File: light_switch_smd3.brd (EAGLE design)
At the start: 37.1 x 45.2 mm, 17 parts, among them J2 SW1, T1 BT136, U1 LM1117

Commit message: light switch version 6 minor adjustments
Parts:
- removed AC, LAMP: DG306-5.0, myblog_library:DG306-PCKG
- added AC+LAMP: DG350-3.5-03P, myblog_library:DG350-3.5-03P
- moved R1 1.40 mm to (3.11, 10.9)
- moved R2 1.10 mm to (5.33, 10.9)
- moved U$2 0.94 mm to (10.8, 4.59)
- moved R5 0.80 mm to (7.49, 10.9)
- moved R6 0.61 mm to (9.81, 11.0)
- moved R4 0.60 mm to (12.3, 10.9)
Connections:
- net N$11: now also AC+LAMP.P$2; no longer AC.P$1, LAMP.P$2
- net N$12: now also AC+LAMP.P$3; no longer AC.P$2
- net N$8: now also AC+LAMP.P$1; no longer LAMP.P$1
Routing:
- net N$32: track 164.1 -> 151.4 mm
- net N$31: track 164.1 -> 151.6 mm
- net N$2: track 13.5 -> 7.16 mm
- net N$3: track 72.6 -> 67.1 mm
- net N$11: track 23.5 -> 19.0 mm
- net GND: track 7.86 -> 12.1 mm
- net N$12: track 24.8 -> 21.2 mm
- net N$4: track 17.9 -> 14.4 mm
- net N$8: track 18.8 -> 17.7 mm
- net N$1: track 16.8 -> 15.8 mm
- net N$5: track 12.0 -> 11.0 mm
- net N$9: track 6.99 -> 6.39 mm
- net N$14: track 4.20 -> 3.70 mm
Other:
- board size 37.1 x 45.2 mm -> 36.5 x 40.3 mm
- board text added: "Hristo Borisov Light Switch Prototype Rev. 0.6"
- board text removed: "Hristo Borisov Light Switch Prototype Rev. 0.5"

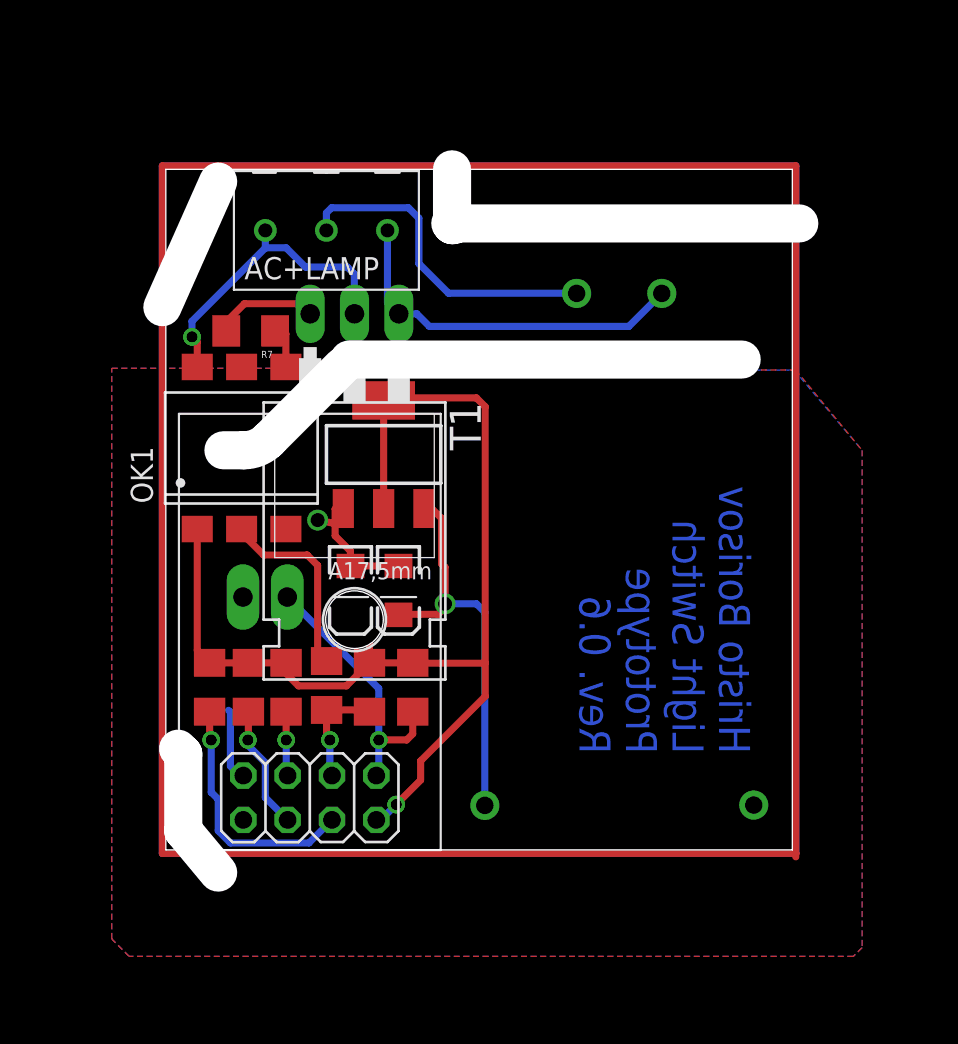
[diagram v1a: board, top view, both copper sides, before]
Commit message: Changing the BT136 device
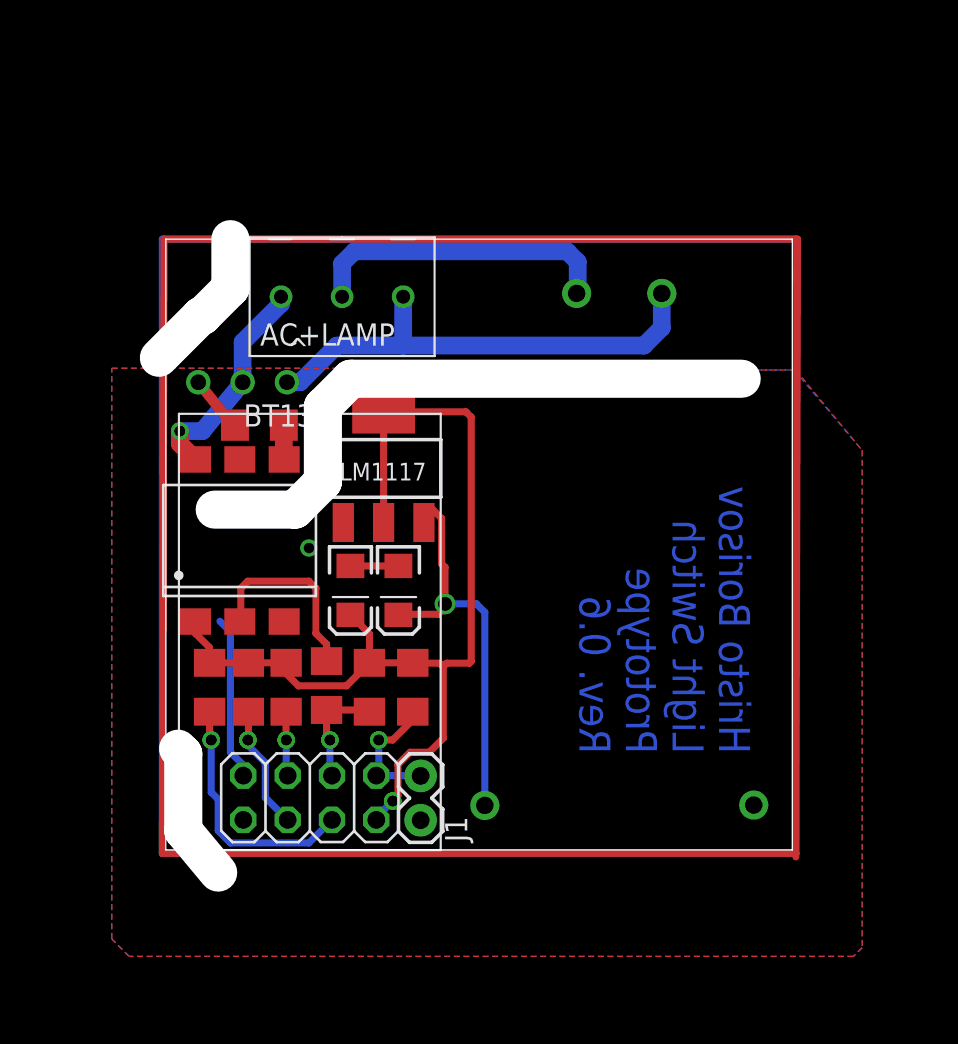
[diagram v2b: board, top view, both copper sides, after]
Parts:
- removed J2: SW1, SparkFun-Connectors:1X02_LONGPADS
- removed T1: BT136, triac:TO220AB
- removed U1: LM1117, SparkFun-PowerIC:SOT223
- added BT136: BT136, myblog_library:BT136-PKG
- added J1: (no value), SparkFun-Connectors:1X02
- added LM1117: LM1117, SparkFun-PowerIC:SOT223
- moved R7 5.42 mm to (5.96, 25.9)
- moved OK1 5.30 mm to (4.84, 19.3)
- moved AC+LAMP 3.91 mm to (10.7, 33.3)
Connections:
- net GND: now also J1.1, LM1117.1; no longer J2.1, U1.1
- net N$1: now also J1.2; no longer J2.2
- net N$12: now also BT136.T1; no longer T1.1
- net N$13: now also LM1117.3; no longer U1.3
- net N$3: now also LM1117.2; no longer U1.2
- net N$6: now also BT136.G; no longer T1.3
- net N$8: now also BT136.T2; no longer T1.2
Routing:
- net N$32: track 151.4 -> 143.0 mm
- net N$31: track 151.6 -> 143.2 mm
- net N$1: track 15.8 -> 7.54 mm
- net N$3: track 67.1 -> 59.0 mm
- net N$12: track 21.2 -> 27.5 mm
- net N$8: track 17.7 -> 12.7 mm
- net N$6: track 6.00 -> 3.29 mm
- net N$11: track 19.0 -> 17.8 mm
- net N$7: track 2.53 -> 1.97 mm
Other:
- board size 36.5 x 40.3 mm -> 36.3 x 36.3 mm

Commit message: Rev. 0.7 - Light Switch is minified and the silkscreen is cleared
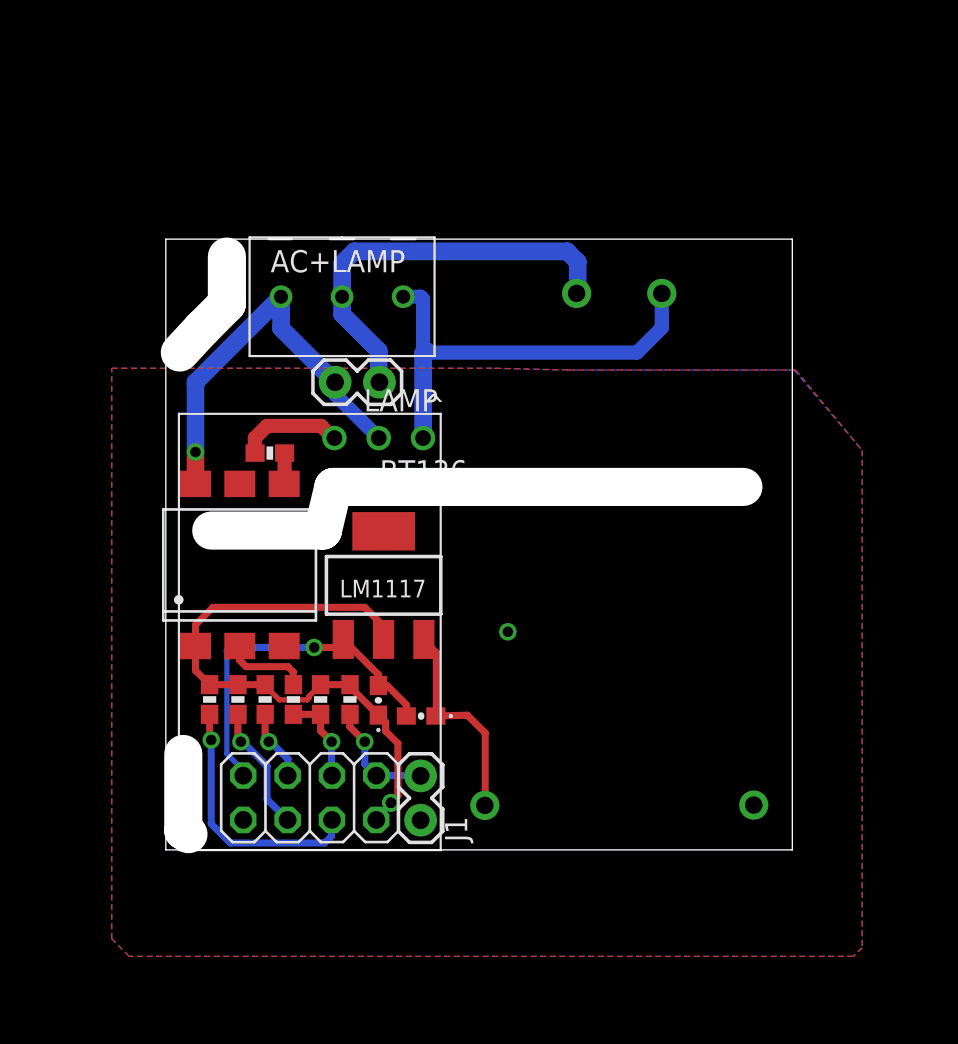
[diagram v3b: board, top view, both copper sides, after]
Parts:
- added LAMP: (no value), SparkFun-Connectors:1X02
- C1, C2: device SparkFun-Capacitors:EIA3216 -> SparkFun-Capacitors:0603-POL
- R1, R2, R3, R4, R5, R6, R7: device SparkFun-Resistors:1206 -> SparkFun-Resistors:0603-RES
- moved BT136 8.43 mm to (12.8, 25.2)
- moved C2 7.32 mm to (15.2, 9.27), turned to 0 degrees
- moved LM1117 6.70 mm to (13.1, 16.8)
- moved C1 6.50 mm to (12.8, 10.2)
- moved R3 3.67 mm to (11.2, 10.2)
- moved R4 2.89 mm to (9.47, 10.2)
- moved R6 2.06 mm to (7.91, 10.2)
- moved R7 1.71 mm to (6.56, 24.3)
- moved OK1 1.40 mm to (4.84, 17.9)
- moved R5 1.39 mm to (6.29, 10.2)
- moved R2 0.92 mm to (4.73, 10.2)
- moved R1 0.70 mm to (3.11, 10.2)
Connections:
- net GND: now also C1.K, C2.K; no longer C1.C, C2.C
- net N$11: now also LAMP.2
- net N$8: now also LAMP.1
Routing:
- net N$31: track 143.2 -> 0.00 mm
- net N$32: track 143.0 -> 0.00 mm
- net N$3: track 59.0 -> 34.4 mm
- net N$13: track 23.3 -> 12.1 mm, vias 1 -> 0
- net N$8: track 12.7 -> 23.2 mm
- net GND: track 12.1 -> 20.7 mm, vias 1 -> 2
- net N$5: track 11.0 -> 4.89 mm
- net N$11: track 17.8 -> 23.6 mm
- net N$6: track 3.29 -> 6.00 mm
- net N$12: track 27.5 -> 25.4 mm
- net N$9: track 6.39 -> 5.34 mm
- net N$1: track 7.54 -> 6.68 mm
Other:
- board size 36.3 x 36.3 mm -> 35.9 x 35 mm
- board text added: "Hristo Borisov Light Switch Prototype Rev. 0.7"
- board text removed: "Hristo Borisov Light Switch Prototype Rev. 0.6"

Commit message: Rev 0.8 - pcb shrinked a bit.
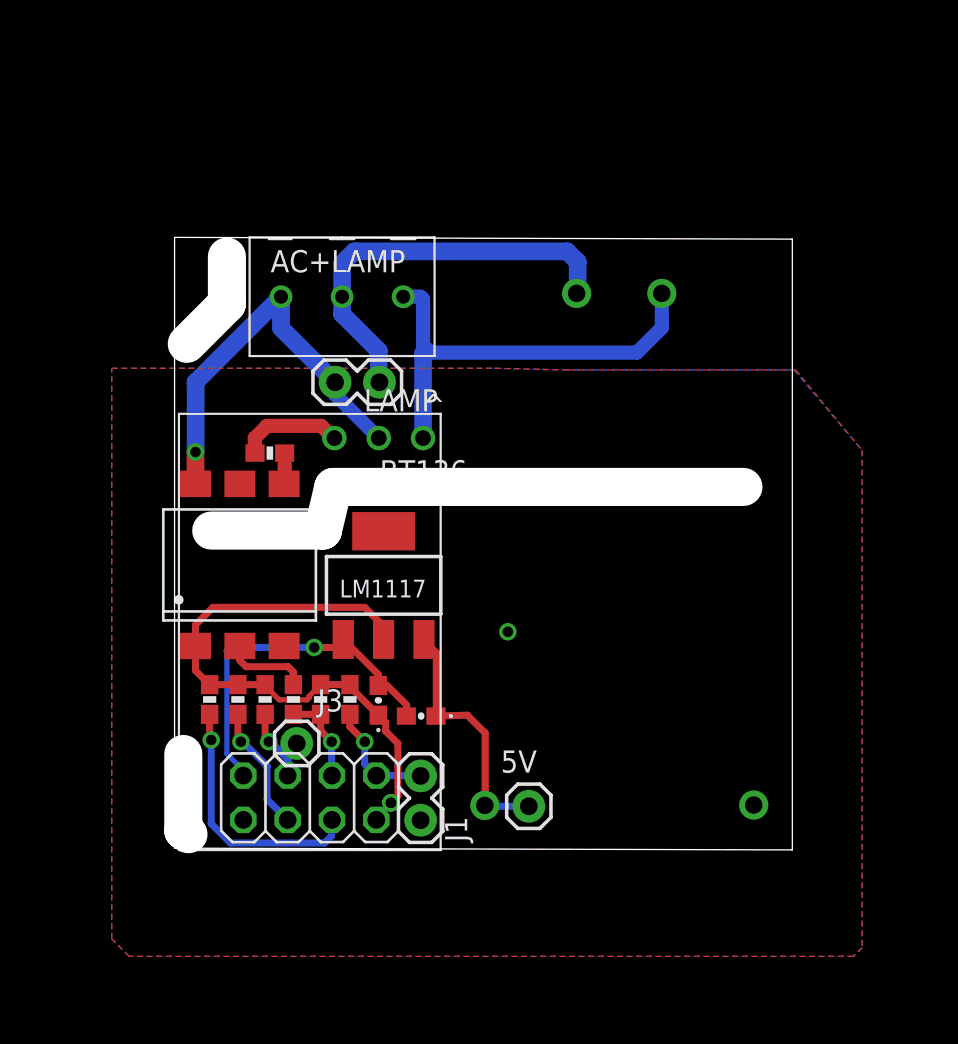
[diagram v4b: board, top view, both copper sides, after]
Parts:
- added 5V, J3: (no value), SparkFun-Connectors:1X01
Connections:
- net N$13: now also 5V.1
- net N$14: now also J3.1
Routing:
- net N$13: track 12.1 -> 14.7 mm
- net N$14: track 4.12 -> 6.48 mm
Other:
- board size 35.9 x 35 mm -> 35.4 x 35.1 mm
- board text added: "Hristo Borisov Light Switch Prototype Rev. 0.8"
- board text removed: "Hristo Borisov Light Switch Prototype Rev. 0.7"
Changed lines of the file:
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@@
 <board>
 <plain>
-<wire x1="0.6" y1="1.6" x2="36.5" y2="1.6" width="0" layer="20"/>
+<wire x1="1.1" y1="1.7" x2="36.5" y2="1.6" width="0" layer="20"/>
 <wire x1="36.5" y1="1.6" x2="36.5" y2="36.6" width="0" layer="20"/>
-<wire x1="36.5" y1="36.6" x2="0.6" y2="36.6" width="0" layer="20"/>
-<wire x1="0.6" y1="36.6" x2="0.6" y2="1.6" width="0" layer="20"/>
+<wire x1="36.5" y1="36.6" x2="1.1" y2="36.7" width="0" layer="20"/>
+<wire x1="1.1" y1="36.7" x2="1.1" y2="1.7" width="0" layer="20"/>
 <wire x1="1.9" y1="2.5" x2="1.6" y2="2.7" width="2.1844" layer="46"/>
 <wire x1="1.6" y1="2.7" x2="1.6" y2="7.1" width="2.1844" layer="46"/>
 <wire x1="4.1" y1="35.6" x2="4.1" y2="32.9" width="2.1844" layer="46"/>
-<wire x1="4.1" y1="32.9" x2="2.7" y2="31.5" width="2.1844" layer="46"/>
-<wire x1="2.7" y1="31.5" x2="1.4" y2="30.1" width="2.1844" layer="46"/>
+<wire x1="4.1" y1="32.9" x2="1.8" y2="30.6" width="2.1844" layer="46"/>
 <wire x1="33.7" y1="22.4" x2="10.2" y2="22.4" width="2.1844" layer="46"/>
 <wire x1="10.2" y1="22.4" x2="9.6" y2="19.9" width="2.1844" layer="46"/>
@@
 Light Switch
 Prototype
-Rev. 0.7</text>
+Rev. 0.8</text>
 </plain>
 <attributes>
@@
 <attribute name="VALUE" x="9.03" y="25.225" size="1.27" layer="27"/>
 </element>
+<element name="5V" library="SparkFun-Connectors" package="1X01" value="" x="21.4" y="4.1" smashed="yes">
+<attribute name="NAME" x="19.7938" y="6.0288" size="1.27" layer="25"/>
+<attribute name="VALUE" x="20.13" y="0.925" size="1.27" layer="27"/>
+</element>
+<element name="J3" library="SparkFun-Connectors" package="1X01" value="" x="8.1" y="7.7"/>
 </elements>
 <signals>
@@
 <wire x1="16.1" y1="12.9" x2="16.1" y2="9.29" width="0.4064" layer="1"/>
 <wire x1="16.1" y1="9.29" x2="16.08" y2="9.27" width="0.4064" layer="1"/>
+<contactref element="5V" pad="1"/>
+<wire x1="21.4" y1="4.1" x2="18.88" y2="4.1" width="0.4064" layer="16"/>
+<wire x1="18.88" y1="4.1" x2="18.88" y2="4.15" width="0.4064" layer="16"/>
 </signal>
 <signal name="N$1">
@@
 <wire x1="15.18" y1="5.86" x2="15.2" y2="5.84" width="0.4064" layer="16"/>
 </signal>
-<signal name="N$4">
+<signal name="N$9">
+<contactref element="R6" pad="1"/>
+<contactref element="R4" pad="2"/>
+<contactref element="U$2" pad="4"/>
+<wire x1="7.91" y1="9.37" x2="9.47" y2="9.37" width="0.4064" layer="1"/>
+<wire x1="9.47" y1="9.37" x2="9.47" y2="8.43" width="0.4064" layer="1"/>
+<wire x1="9.47" y1="8.43" x2="10.1" y2="7.8" width="0.4064" layer="1"/>
+<via x="10.1" y="7.8" extent="1-16" drill="0.6"/>
+<wire x1="10.1" y1="7.8" x2="10.1" y2="5.88" width="0.4064" layer="16"/>
+<wire x1="10.1" y1="5.88" x2="10.12" y2="5.86" width="0.4064" layer="16"/>
+</signal>
+<signal name="N$14">
+<contactref element="U$2" pad="6"/>
+<contactref element="R5" pad="1"/>
+<wire x1="6.29" y1="9.37" x2="6.29" y2="8.01" width="0.4064" layer="1"/>
+<wire x1="6.29" y1="8.01" x2="6.5" y2="7.8" width="0.4064" layer="1"/>
+<via x="6.5" y="7.8" extent="1-16" drill="0.6"/>
+<wire x1="6.5" y1="7.8" x2="6.6" y2="7.8" width="0.4064" layer="16"/>
+<wire x1="6.6" y1="7.8" x2="7.6" y2="6.8" width="0.4064" layer="16"/>
+<wire x1="7.6" y1="6.8" x2="7.6" y2="5.88" width="0.4064" layer="16"/>
+<wire x1="7.6" y1="5.88" x2="7.58" y2="5.86" width="0.4064" layer="16"/>
+<contactref element="J3" pad="1"/>
+<wire x1="8.1" y1="7.7" x2="7.58" y2="7.7" width="0.4064" layer="16"/>
+<wire x1="7.58" y1="7.7" x2="7.58" y2="5.86" width="0.4064" layer="16"/>
+</signal>
+<signal name="N$2">
+<contactref element="U$2" pad="5"/>
+<contactref element="R2" pad="1"/>
+<wire x1="4.73" y1="9.37" x2="4.73" y2="7.97" width="0.4064" layer="1"/>
+<wire x1="4.73" y1="7.97" x2="4.9" y2="7.8" width="0.4064" layer="1"/>
+<via x="4.9" y="7.8" extent="1-16" drill="0.6" diameter="0.8128"/>
+<wire x1="4.9" y1="7.8" x2="5" y2="7.8" width="0.4064" layer="16"/>
+<wire x1="5" y1="7.8" x2="6.4" y2="6.4" width="0.4064" layer="16"/>
+<wire x1="6.4" y1="6.4" x2="6.4" y2="4.5" width="0.4064" layer="16"/>
+<wire x1="6.4" y1="4.5" x2="7.58" y2="3.32" width="0.4064" layer="16"/>
+</signal>
+<signal name="N$19">
+</signal>
+<signal name="N$20">
+</signal>
+<signal name="N$21">
+</signal>
+<signal name="N$10">
+</signal>
+<signal name="N$15">
+</signal>
+<signal name="N$18">
+</signal>
+<signal name="N$22">
+</signal>
+<signal name="N$23">
+</signal>
+<signal name="N$35">
+</signal>
+<signal name="N$38">
+</signal>
+<signal name="N$39">
+</signal>
+<signal name="N$40">
+</signal>
+<signal name="N$41">
+</signal>
+<signal name="N$31">
+</signal>
+<signal name="N$32">
+</signal>
+<signal name="N$17">
+</signal>
+<signal name="N$25">
+</signal>
+<signal name="N$6">
+<contactref element="R7" pad="2"/>
+<contactref element="BT136" pad="G"/>
+<wire x1="10.26" y1="25.2" x2="10.2" y2="25.2" width="0.8128" layer="1"/>
+<wire x1="10.2" y1="25.2" x2="9.5" y2="25.9" width="0.8128" layer="1"/>
+<wire x1="9.5" y1="25.9" x2="6.4" y2="25.9" width="0.8128" layer="1"/>
+<wire x1="6.4" y1="25.9" x2="5.7" y2="25.2" width="0.8128" layer="1"/>
+<wire x1="5.7" y1="25.2" x2="5.7" y2="24.35" width="0.8128" layer="1"/>
+<wire x1="5.7" y1="24.35" x2="5.71" y2="24.34" width="0.8128" layer="1"/>
+</signal>
+<signal name="N$16">
+<via x="13.5" y="4.3" extent="1-16" drill="0.6"/>
+</signal>
+<signal name="N$24">
+</signal>
+<signal name="N$26">
 <contactref element="R1" pad="2"/>
 <contactref element="U$2" pad="3"/>
@@
 <wire x1="10.1" y1="3.3" x2="10.12" y2="3.32" width="0.4064" layer="16"/>
 </signal>
-<signal name="N$9">
-<contactref element="R6" pad="1"/>
-<contactref element="R4" pad="2"/>
-<contactref element="U$2" pad="4"/>
-<wire x1="7.91" y1="9.37" x2="9.47" y2="9.37" width="0.4064" layer="1"/>
-<wire x1="9.47" y1="9.37" x2="9.47" y2="8.43" width="0.4064" layer="1"/>
-<wire x1="9.47" y1="8.43" x2="10.1" y2="7.8" width="0.4064" layer="1"/>
-<via x="10.1" y="7.8" extent="1-16" drill="0.6"/>
-<wire x1="10.1" y1="7.8" x2="10.1" y2="5.88" width="0.4064" layer="16"/>
-<wire x1="10.1" y1="5.88" x2="10.12" y2="5.86" width="0.4064" layer="16"/>
-</signal>
-<signal name="N$14">
-<contactref element="U$2" pad="6"/>
-<contactref element="R5" pad="1"/>
-<wire x1="6.29" y1="9.37" x2="6.29" y2="8.01" width="0.4064" layer="1"/>
-<wire x1="6.29" y1="8.01" x2="6.5" y2="7.8" width="0.4064" layer="1"/>
-<via x="6.5" y="7.8" extent="1-16" drill="0.6"/>
-<wire x1="6.5" y1="7.8" x2="6.6" y2="7.8" width="0.4064" layer="16"/>
-<wire x1="6.6" y1="7.8" x2="7.6" y2="6.8" width="0.4064" layer="16"/>
-<wire x1="7.6" y1="6.8" x2="7.6" y2="5.88" width="0.4064" layer="16"/>
-<wire x1="7.6" y1="5.88" x2="7.58" y2="5.86" width="0.4064" layer="16"/>
-</signal>
-<signal name="N$2">
-<contactref element="U$2" pad="5"/>
-<contactref element="R2" pad="1"/>
-<wire x1="4.73" y1="9.37" x2="4.73" y2="7.97" width="0.4064" layer="1"/>
-<wire x1="4.73" y1="7.97" x2="4.9" y2="7.8" width="0.4064" layer="1"/>
-<via x="4.9" y="7.8" extent="1-16" drill="0.6" diameter="0.8128"/>
-<wire x1="4.9" y1="7.8" x2="5" y2="7.8" width="0.4064" layer="16"/>
-<wire x1="5" y1="7.8" x2="6.4" y2="6.4" width="0.4064" layer="16"/>
-<wire x1="6.4" y1="6.4" x2="6.4" y2="4.5" width="0.4064" layer="16"/>
-<wire x1="6.4" y1="4.5" x2="7.58" y2="3.32" width="0.4064" layer="16"/>
-</signal>
-<signal name="N$19">
-</signal>
-<signal name="N$20">
-</signal>
-<signal name="N$21">
-</signal>
-<signal name="N$10">
-</signal>
-<signal name="N$15">
-</signal>
-<signal name="N$18">
-</signal>
-<signal name="N$22">
-</signal>
-<signal name="N$23">
-</signal>
-<signal name="N$35">
-</signal>
-<signal name="N$38">
-</signal>
-<signal name="N$39">
-</signal>
-<signal name="N$40">
-</signal>
-<signal name="N$41">
-</signal>
-<signal name="N$31">
-</signal>
-<signal name="N$32">
-</signal>
-<signal name="N$17">
-</signal>
-<signal name="N$25">
-</signal>
-<signal name="N$6">
-<contactref element="R7" pad="2"/>
-<contactref element="BT136" pad="G"/>
-<wire x1="10.26" y1="25.2" x2="10.2" y2="25.2" width="0.8128" layer="1"/>
-<wire x1="10.2" y1="25.2" x2="9.5" y2="25.9" width="0.8128" layer="1"/>
-<wire x1="9.5" y1="25.9" x2="6.4" y2="25.9" width="0.8128" layer="1"/>
-<wire x1="6.4" y1="25.9" x2="5.7" y2="25.2" width="0.8128" layer="1"/>
-<wire x1="5.7" y1="25.2" x2="5.7" y2="24.35" width="0.8128" layer="1"/>
-<wire x1="5.7" y1="24.35" x2="5.71" y2="24.34" width="0.8128" layer="1"/>
-</signal>
-<signal name="N$16">
-<via x="13.5" y="4.3" extent="1-16" drill="0.6"/>
-</signal>
-<signal name="N$24">
-</signal>
 </signals>
